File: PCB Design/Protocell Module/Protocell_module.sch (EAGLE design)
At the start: 5 parts, among them X1 RJ45-8X

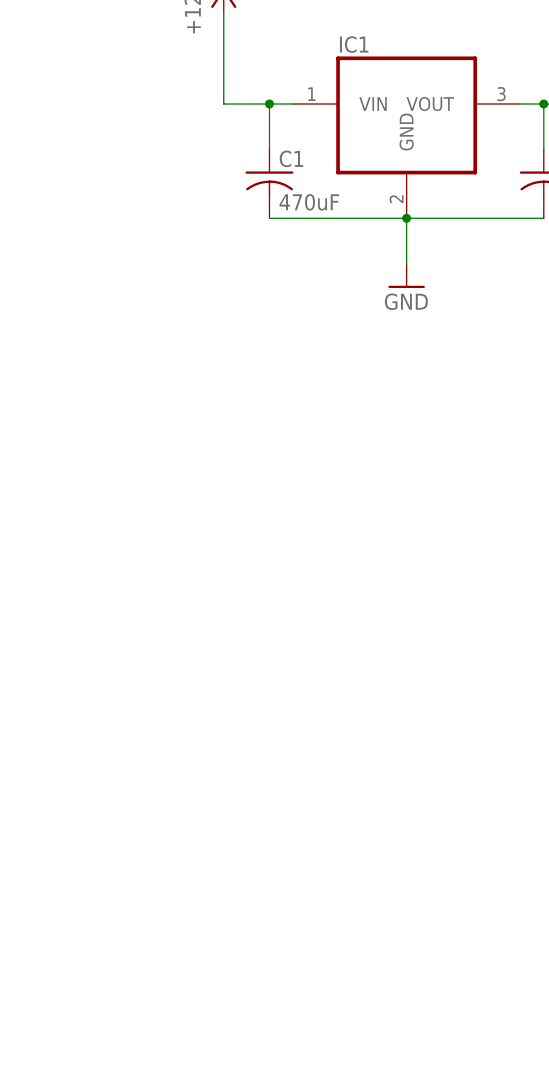
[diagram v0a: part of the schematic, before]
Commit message: Added Exar and TI libraries
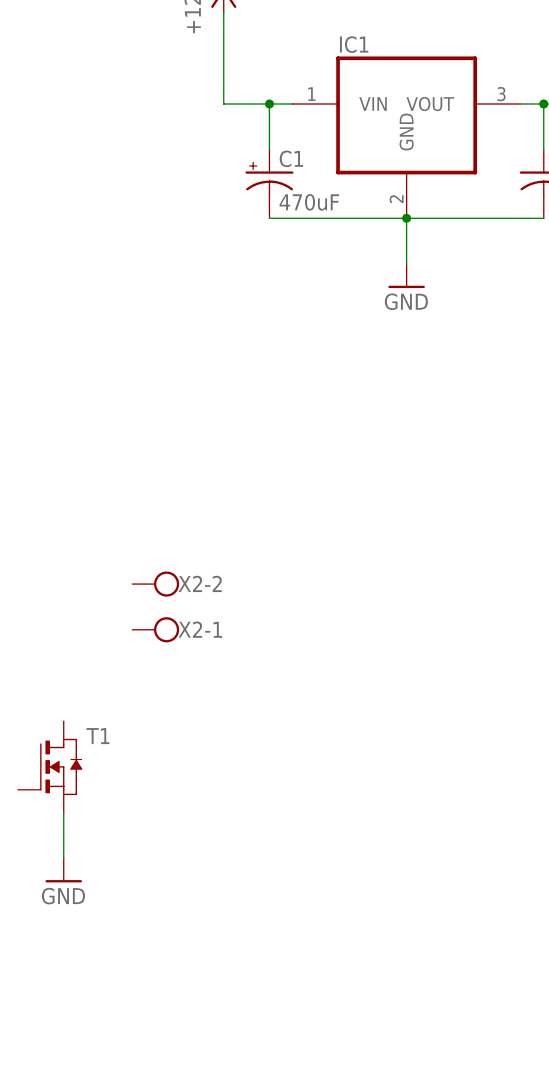
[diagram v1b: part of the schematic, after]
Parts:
- added T1: (no value), CBLA_Test_bed_Library:NTD5867NLT4G
- added X2: (no value), con-wago-500:W237-102
- C1: device rcl:C-USC0603 -> rcl:CPOL-USE5-10.5
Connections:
- net +12V: now also C1.+; no longer C1.1
- net GND: now also C1.-, T1.S; no longer C1.2
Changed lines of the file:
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@@
 <part name="P+2" library="supply1" deviceset="+12V" device=""/>
 <part name="GND1" library="supply1" deviceset="GND" device=""/>
-<part name="C1" library="rcl" deviceset="C-US" device="C0603" value="470uF"/>
+<part name="C1" library="rcl" deviceset="CPOL-US" device="E5-10.5" value="470uF"/>
 <part name="C2" library="rcl" deviceset="C-US" device="C0603" value="1uF"/>
 <part name="X1" library="CBLA_Test_bed_Library" deviceset="RJ45" device="" technology="-8X"/>
 <part name="J1" library="CBLA_Test_bed_Library" deviceset="558872-1" device=""/>
+<part name="T1" library="CBLA_Test_bed_Library" deviceset="NTD5867NL" device="T4G"/>
+<part name="X2" library="con-wago-500" deviceset="W237-102" device=""/>
+<part name="GND2" library="supply1" deviceset="GND" device=""/>
 </parts>
 <sheets>
@@
 <instance part="X1" gate="G$1" x="157.48" y="160.02"/>
 <instance part="J1" gate="G$1" x="157.48" y="116.84"/>
+<instance part="T1" gate="A" x="53.34" y="60.96"/>
+<instance part="X2" gate="-1" x="66.04" y="76.2" rot="R180"/>
+<instance part="X2" gate="-2" x="66.04" y="81.28" rot="R180"/>
+<instance part="GND2" gate="1" x="53.34" y="48.26"/>
 </instances>
 <busses>
@@
 <pinref part="IC1" gate="G$1" pin="VIN"/>
 <wire x1="71.12" y1="134.62" x2="76.2" y2="134.62" width="0.1524" layer="91"/>
-<pinref part="C1" gate="G$1" pin="1"/>
+<pinref part="C1" gate="G$1" pin="+"/>
 <wire x1="76.2" y1="134.62" x2="78.74" y2="134.62" width="0.1524" layer="91"/>
 <wire x1="76.2" y1="134.62" x2="76.2" y2="129.54" width="0.1524" layer="91"/>
@@
 <pinref part="GND1" gate="1" pin="GND"/>
 <wire x1="91.44" y1="121.92" x2="91.44" y2="116.84" width="0.1524" layer="91"/>
-<pinref part="C1" gate="G$1" pin="2"/>
+<pinref part="C1" gate="G$1" pin="-"/>
 <wire x1="76.2" y1="121.92" x2="91.44" y2="121.92" width="0.1524" layer="91"/>
 <junction x="91.44" y="121.92"/>
@@
 <label x="137.16" y="119.38" size="1.778" layer="95"/>
 </segment>
+<segment>
+<pinref part="T1" gate="A" pin="S"/>
+<pinref part="GND2" gate="1" pin="GND"/>
+<wire x1="53.34" y1="55.88" x2="53.34" y2="50.8" width="0.1524" layer="91"/>
+</segment>
 </net>

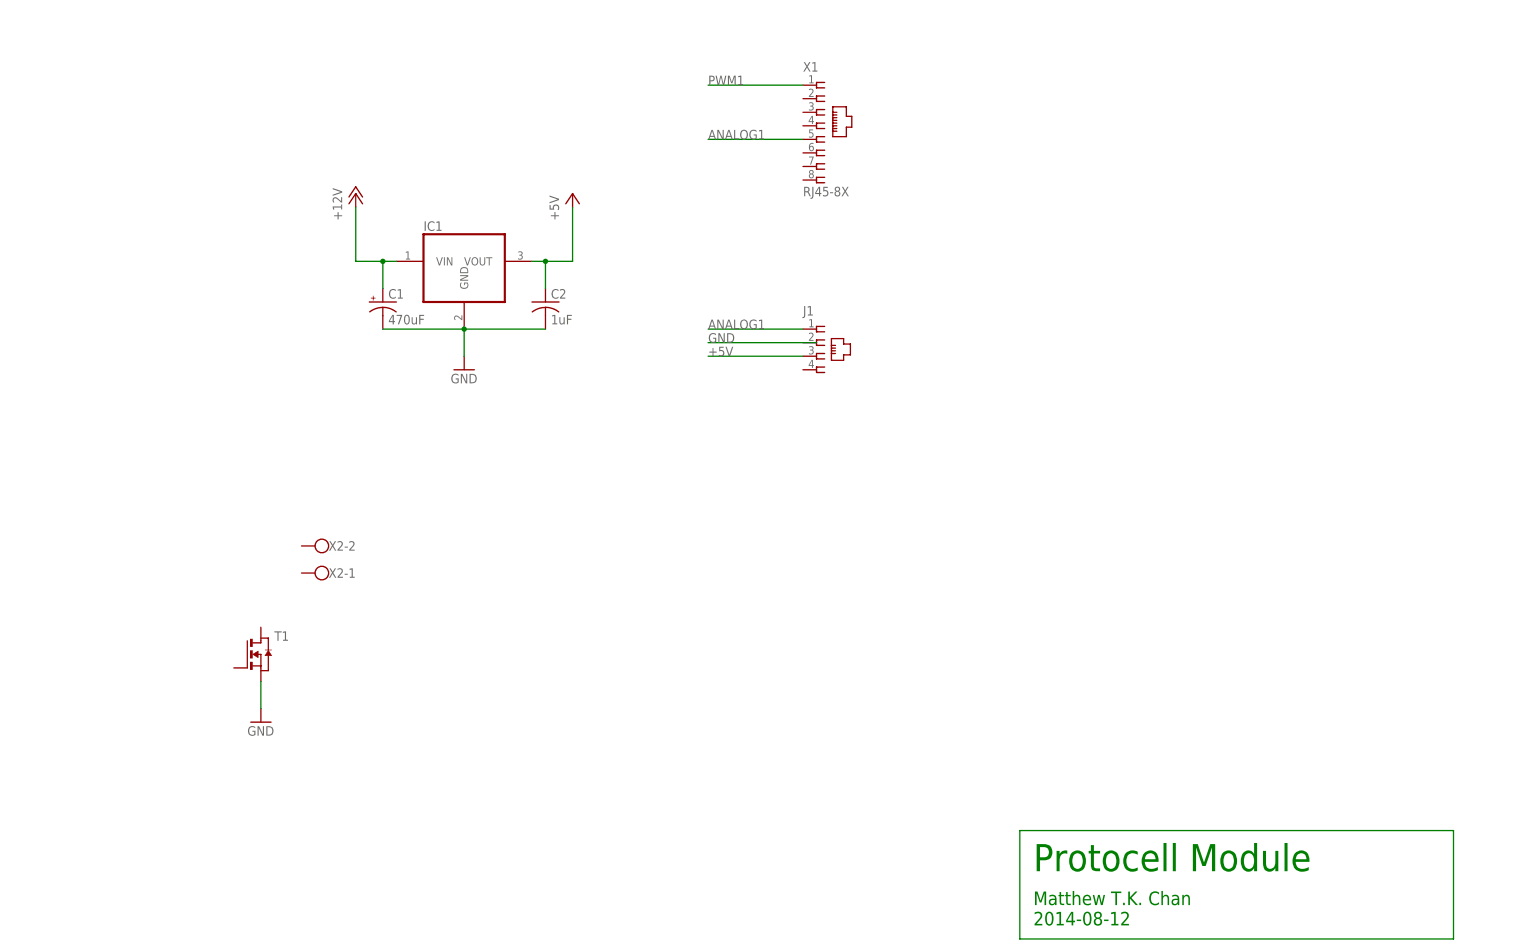
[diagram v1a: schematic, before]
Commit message: Finished schematic and part placements
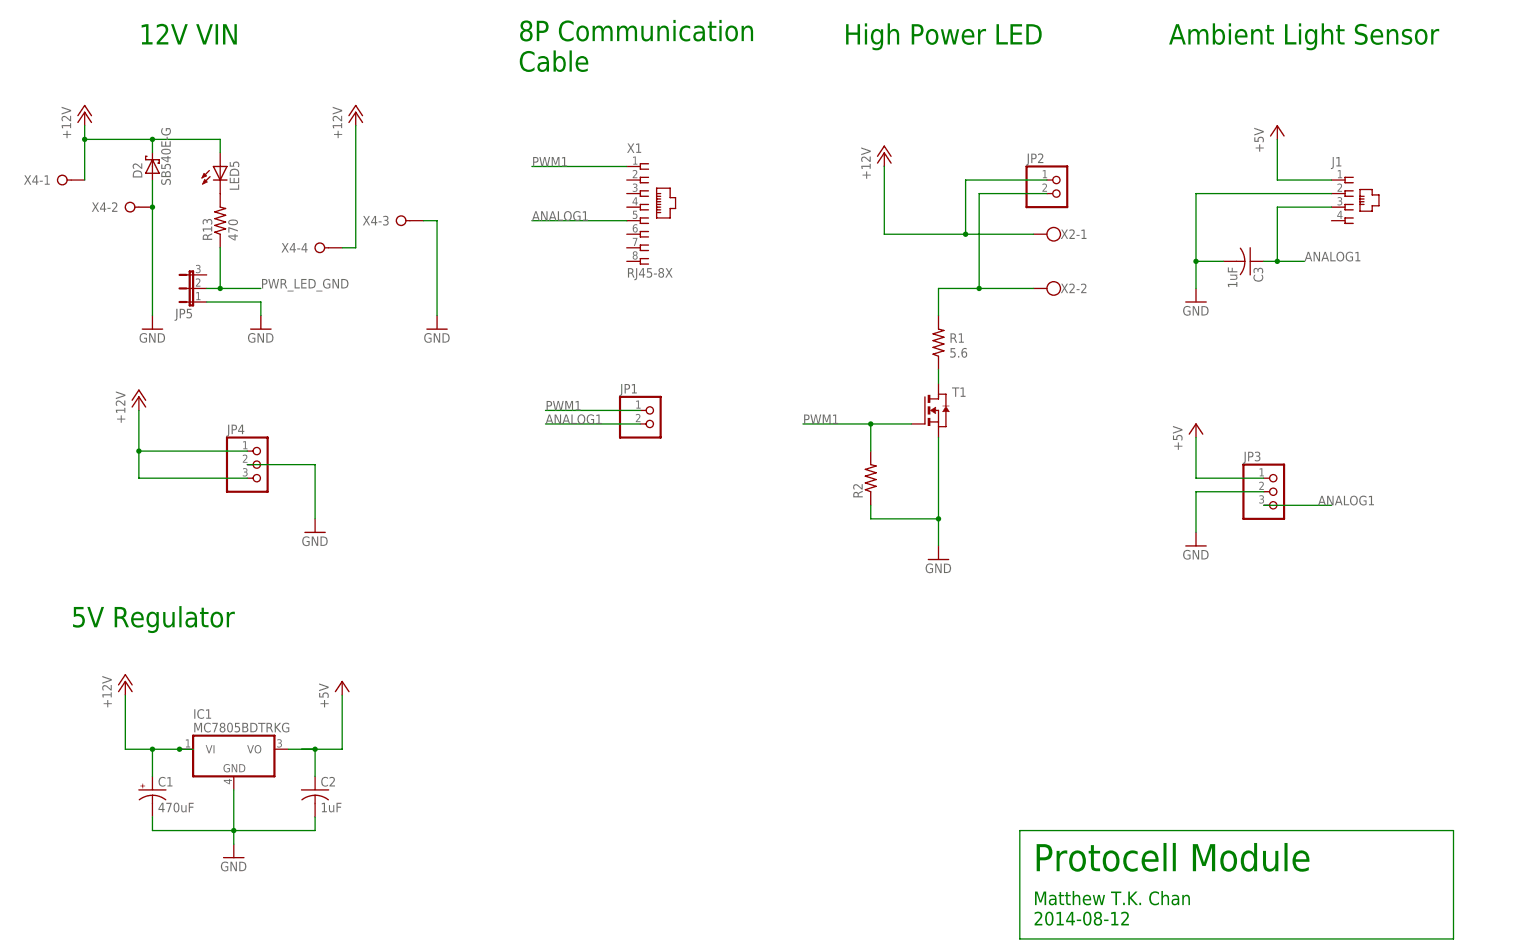
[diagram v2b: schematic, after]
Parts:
- added C3: 1uF, rcl:C-USC0603
- added D2: SB540E-G, CBLA_Test_bed_Library:SB540E-G
- added JP1, JP2: (no value), CBLA_Test_bed_Library:PINHD-1X2/90
- added JP3, JP4: (no value), CBLA_Test_bed_Library:PINHD-1X3/90
- added JP5: (no value), jumper:JP2E
- added LED5: (no value), led:LEDSML1206
- added R1: 5.6, CBLA_Test_bed_Library:SQP500JB-5R6
- added R13: 470, CBLA_Test_bed_Library:R-US_R0603
- added R2: (no value), CBLA_Test_bed_Library:R-US_R0603
- added X4: (no value), con-wago-508:W237-04P
- IC1: value (none) -> MC7805BDTRKG; device CBLA_Test_bed_Library:REG11175.0VDT -> CBLA_Test_bed_Library:MC7805BDTRKG
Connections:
- new net N$1: R1.1, T1.D
- new net N$10: LED5.C, R13.2
- new net N$3: JP2.2, R1.2, X2-2.KL
- new net PWR_LED_GND: JP5.2, R13.1
- net +12V: now also D2.C, IC1.VI, JP2.1, JP4.1, JP4.3, LED5.A, X2-1.KL, X4-1.KL, X4-4.KL; no longer IC1.VIN
- net +5V: now also IC1.VO, J1.1, JP3.1; no longer IC1.VOUT, J1.3
- net ANALOG1: now also C3.1, J1.3, JP1.2, JP3.3; no longer J1.1
- net GND: now also C3.2, D2.A, J1.2, JP3.2, JP4.2, JP5.1, R2.1, X4-2.KL, X4-3.KL
- net PWM1: now also JP1.1, R2.2, T1.G
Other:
- note added: "12V VIN"
- note added: "5V Regulator"
- note added: "8P Communication Cable"
- note added: "Ambient Light Sensor"
- note added: "High Power LED"
- moved on the sheet: C1, C2, IC1, J1, T1, X1, X2-1, X2-2

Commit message: Polished silkscreen on protocell board
also add prefix to a part in library
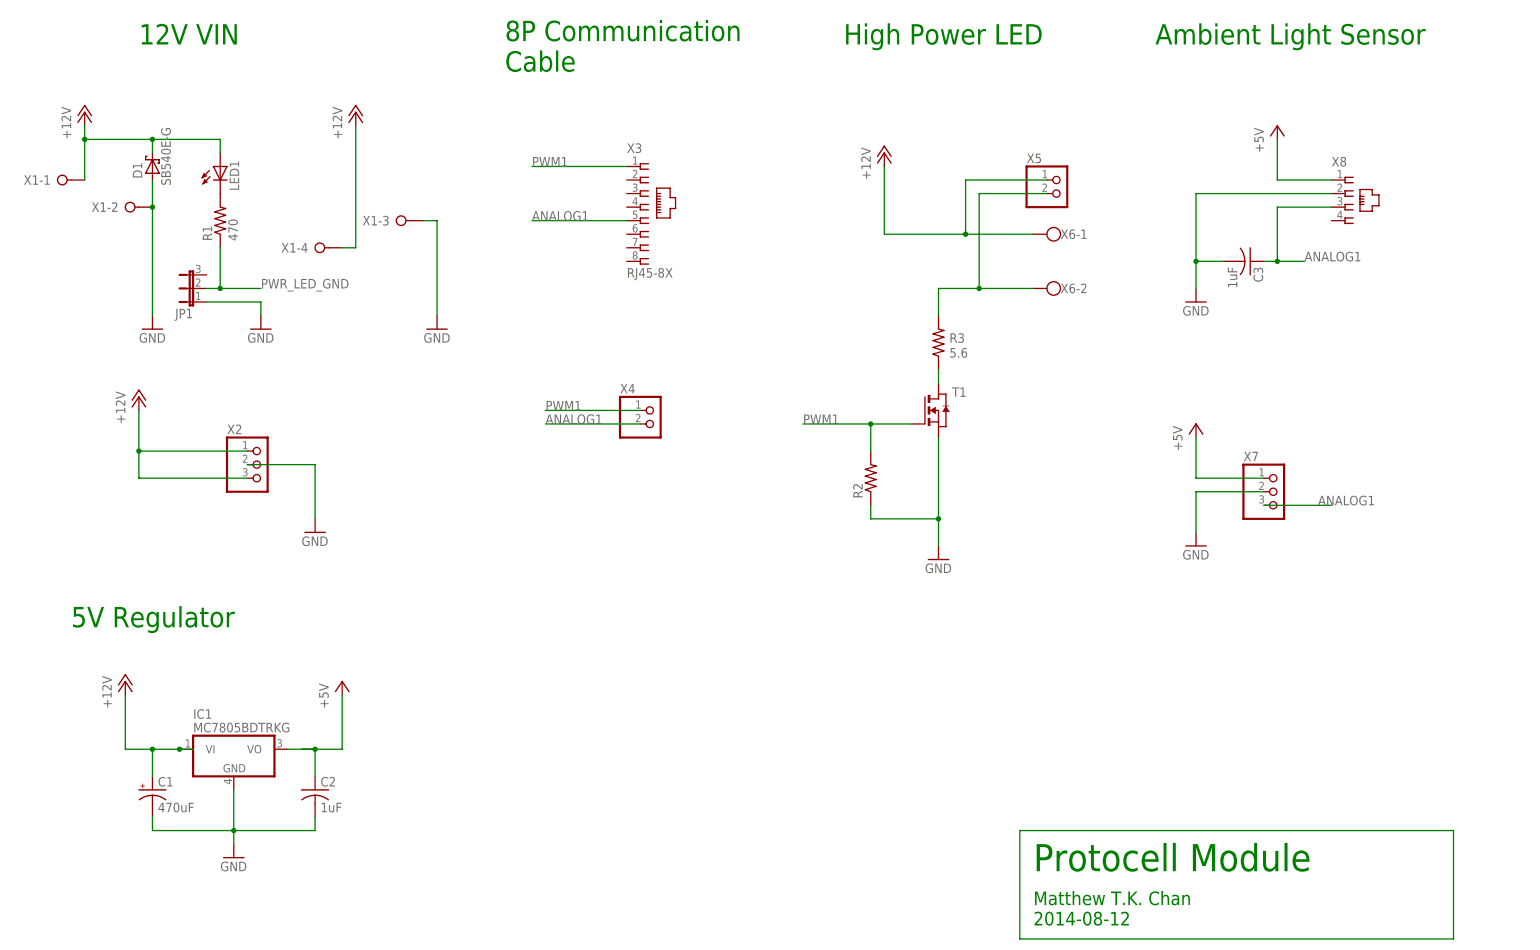
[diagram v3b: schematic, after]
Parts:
- removed JP4: (no value), CBLA_Test_bed_Library:PINHD-1X3/90
- removed JP5: (no value), jumper:JP2E
- removed R13: 470, CBLA_Test_bed_Library:R-US_R0603
- added R3: 5.6, CBLA_Test_bed_Library:SQP500JB-5R6
- added X3: RJ45-8X, CBLA_Test_bed_Library:RJ45-8X
- added X6: (no value), con-wago-500:W237-102
- JP1: device CBLA_Test_bed_Library:PINHD-1X2/90 -> jumper:JP2E
- R1: value 5.6 -> 470; device CBLA_Test_bed_Library:SQP500JB-5R6 -> CBLA_Test_bed_Library:R-US_R0603
- X1: value RJ45-8X -> (none); device CBLA_Test_bed_Library:RJ45-8X -> con-wago-508:W237-04P
- X2: device con-wago-500:W237-102 -> CBLA_Test_bed_Library:PINHD-1X3/90
- X4: device con-wago-508:W237-04P -> CBLA_Test_bed_Library:PINHD-1X2/90
- renumbered D2 to D1, J1 to X8, JP2 to X5, JP3 to X7, LED5 to LED1
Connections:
- net +12V: now also X1-1.KL, X1-4.KL, X2.1, X2.3, X6-1.KL; no longer JP4.1, JP4.3, X2-1.KL, X4-1.KL, X4-4.KL
- net ANALOG1: now also X3.5, X4.2; no longer JP1.2, X1.5
- net GND: now also JP1.1, X1-2.KL, X1-3.KL, X2.2; no longer JP4.2, JP5.1, X4-2.KL, X4-3.KL
- net N$1: now also R3.1; no longer R1.1
- net N$10: now also R1.2; no longer R13.2
- net N$3: now also R3.2, X6-2.KL; no longer R1.2, X2-2.KL
- net PWM1: now also X3.1, X4.1; no longer JP1.1, X1.1
- net PWR_LED_GND: now also JP1.2, R1.1; no longer JP5.2, R13.1
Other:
- moved on the sheet: R1

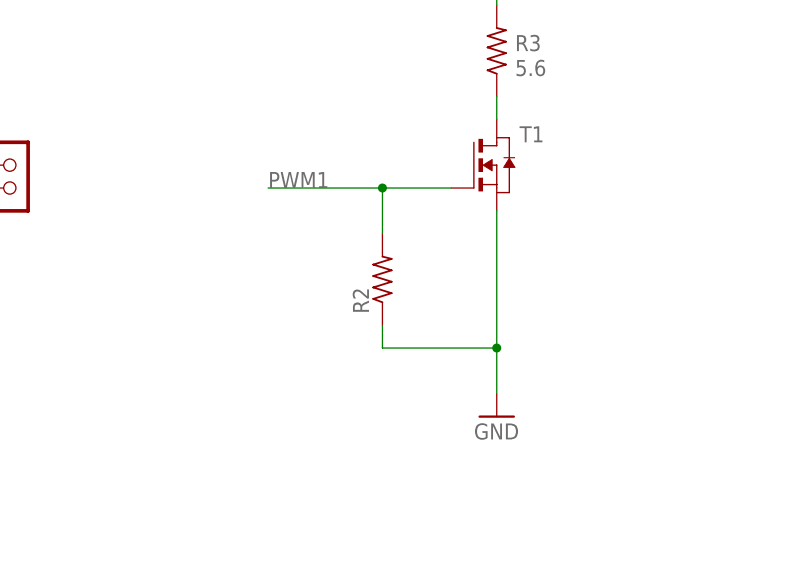
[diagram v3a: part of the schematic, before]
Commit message: Added protocell module component to BOM
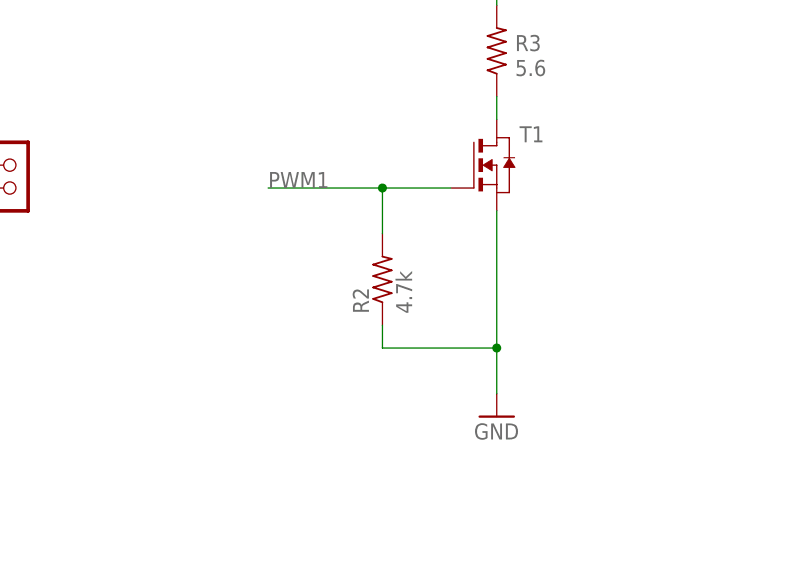
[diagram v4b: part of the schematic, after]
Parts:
- R2: value (none) -> 4.7k
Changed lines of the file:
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@@
 <part name="R3" library="CBLA_Test_bed_Library" deviceset="SQP500" device="JB-5R6" value="5.6"/>
 <part name="P+6" library="supply1" deviceset="+12V" device=""/>
-<part name="R2" library="CBLA_Test_bed_Library" deviceset="R-US_" device="R0603"/>
+<part name="R2" library="CBLA_Test_bed_Library" deviceset="R-US_" device="R0603" value="4.7k"/>
 <part name="C3" library="rcl" deviceset="C-US" device="C0603" value="1uF"/>
 <part name="P+8" library="supply1" deviceset="+5V" device=""/>
